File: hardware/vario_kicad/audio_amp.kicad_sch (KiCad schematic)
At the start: 16 parts

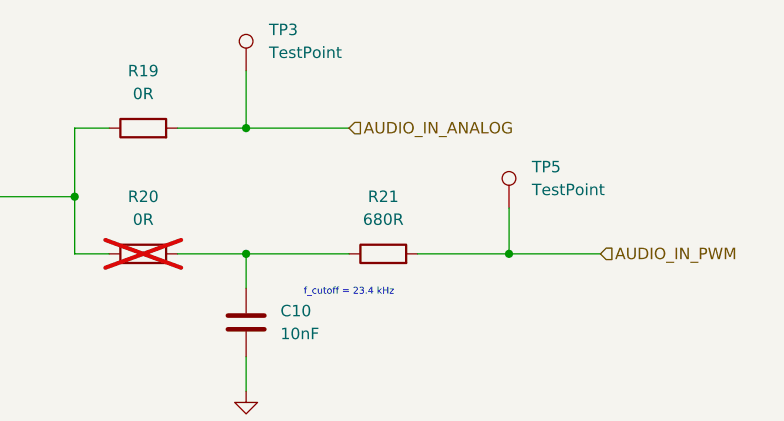
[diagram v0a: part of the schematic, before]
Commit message: remove more testpoints
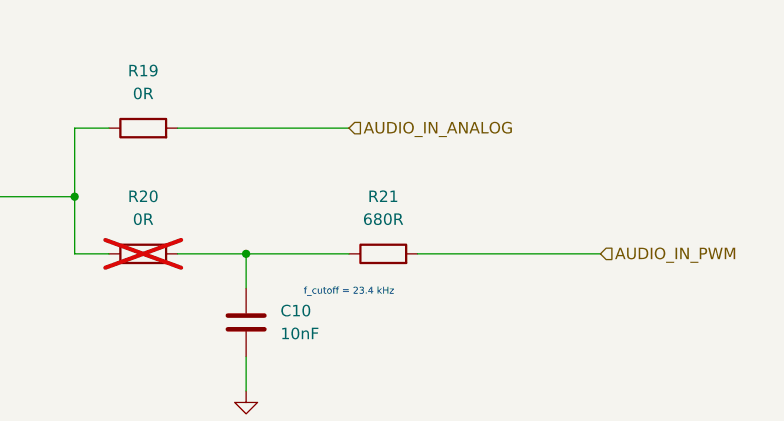
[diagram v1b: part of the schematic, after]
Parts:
- removed TP3, TP5: TestPoint, TestPoint:TestPoint_Pad_D1.0mm, symbol Connector:TestPoint
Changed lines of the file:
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@@
-	)
-	(junction
-		(at 226.06 97.79)
-		(diameter 0)
-		(color 0 0 0 0)
 	)
 	(junction
@@
 	)
 	(junction
-		(at 196.85 83.82)
-		(diameter 0)
-		(color 0 0 0 0)
-	)
-	(junction
 		(at 78.74 115.57)
 		(diameter 0)
@@
 	(wire
 		(pts
-			(xy 226.06 92.71) (xy 226.06 97.79)
-		)
-		(stroke
-			(width 0)
-			(type default)
-		)
-	)
-	(wire
-		(pts
 			(xy 68.58 100.33) (xy 60.96 100.33)
 		)
@@
 	(wire
 		(pts
-			(xy 226.06 97.79) (xy 236.22 97.79)
+			(xy 215.9 97.79) (xy 236.22 97.79)
 		)
 		(stroke
@@
 	(wire
 		(pts
-			(xy 196.85 83.82) (xy 208.28 83.82)
-		)
-		(stroke
-			(width 0)
-			(type default)
-		)
-	)
-	(wire
-		(pts
 			(xy 109.22 115.57) (xy 95.25 115.57)
 		)
@@
 	(wire
 		(pts
-			(xy 215.9 97.79) (xy 226.06 97.79)
-		)
-		(stroke
-			(width 0)
-			(type default)
-		)
-	)
-	(wire
-		(pts
 			(xy 95.25 114.3) (xy 95.25 115.57)
 		)
@@
 	(wire
 		(pts
-			(xy 196.85 77.47) (xy 196.85 83.82)
-		)
-		(stroke
-			(width 0)
-			(type default)
-		)
-	)
-	(wire
-		(pts
 			(xy 177.8 91.44) (xy 177.8 83.82)
 		)
@@
 	(wire
 		(pts
-			(xy 189.23 83.82) (xy 196.85 83.82)
+			(xy 189.23 83.82) (xy 208.28 83.82)
 		)
 		(stroke
@@
 	)
 	(symbol
-		(lib_id "Connector:TestPoint")
-		(at 226.06 92.71 0)
-		(unit 1)
-		(exclude_from_sim no)
-		(in_bom yes)
-		(on_board yes)
-		(dnp no)
-		(fields_autoplaced yes)
-		(property "Reference" "TP5"
-			(at 228.6 88.1379 0)
-			(effects
-				(font
-					(size 1.27 1.27)
-				)
-				(justify left)
-			)
-		)
-		(property "Value" "TestPoint"
-			(at 228.6 90.6779 0)
-			(effects
-				(font
-					(size 1.27 1.27)
-				)
-				(justify left)
-			)
-		)
-		(property "Footprint" "TestPoint:TestPoint_Pad_D1.0mm"
-			(at 231.14 92.71 0)
-			(effects
-				(font
-					(size 1.27 1.27)
-				)
-				(hide yes)
-			)
-		)
-		(property "Datasheet" "~"
-			(at 231.14 92.71 0)
-			(effects
-				(font
-					(size 1.27 1.27)
-				)
-				(hide yes)
-			)
-		)
-		(property "Description" "test point"
-			(at 226.06 92.71 0)
-			(effects
-				(font
-					(size 1.27 1.27)
-				)
-				(hide yes)
-			)
-		)
-		(pin "1"
-		)
-		(instances
-			(project ""
-				(path "/50389aff-b244-451e-8e3a-c5addd2215e1/c1ce8014-8ca1-4d8c-ab67-abb68a6156e7"
-					(reference "TP5")
-					(unit 1)
-				)
-			)
-		)
-	)
-	(symbol
 		(lib_id "New_Library:NS4150B")
 		(at 80.01 97.79 0)
@@
 					(unit 1)
 				)
-			)
-		)
-	)
-	(symbol
-		(lib_id "Connector:TestPoint")
-		(at 196.85 77.47 0)
-		(unit 1)
-		(exclude_from_sim no)
-		(in_bom yes)
-		(on_board yes)
-		(dnp no)
-		(fields_autoplaced yes)
-		(property "Reference" "TP3"
-			(at 199.39 72.8979 0)
-			(effects
-				(font
-					(size 1.27 1.27)
-				)
-				(justify left)
-			)
-		)
-		(property "Value" "TestPoint"
-			(at 199.39 75.4379 0)
-			(effects
-				(font
-					(size 1.27 1.27)
-				)
-				(justify left)
-			)
-		)
-		(property "Footprint" "TestPoint:TestPoint_Pad_D1.0mm"
-			(at 201.93 77.47 0)
-			(effects
-				(font
-					(size 1.27 1.27)
-				)
-				(hide yes)
-			)
-		)
-		(property "Datasheet" "~"
-			(at 201.93 77.47 0)
-			(effects
-				(font
-					(size 1.27 1.27)
-				)
-				(hide yes)
-			)
-		)
-		(property "Description" "test point"
-			(at 196.85 77.47 0)
-			(effects
-				(font
-					(size 1.27 1.27)
-				)
-				(hide yes)
-			)
-		)
-		(pin "1"
-		)
-		(instances
-			(project "vario_kicad"
-				(path "/50389aff-b244-451e-8e3a-c5addd2215e1/c1ce8014-8ca1-4d8c-ab67-abb68a6156e7"
-					(reference "TP3")
-					(unit 1)
-				)

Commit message: use 0402 instead of 0603 for almost all caps
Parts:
- C10, C5, C6, C7, C8, C9: footprint Capacitor_SMD:C_0603_1608Metric -> Capacitor_SMD:C_0402_1005Metric
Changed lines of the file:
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@@
 			)
 		)
-		(property "Footprint" "Capacitor_SMD:C_0603_1608Metric"
+		(property "Footprint" "Capacitor_SMD:C_0402_1005Metric"
 			(at 96.2152 114.3 0)
 			(effects
@@
 			)
 		)
-		(property "Footprint" "Capacitor_SMD:C_0603_1608Metric"
+		(property "Footprint" "Capacitor_SMD:C_0402_1005Metric"
 			(at 53.0352 88.9 0)
 			(effects
@@
 			)
 		)
-		(property "Footprint" "Capacitor_SMD:C_0603_1608Metric"
+		(property "Footprint" "Capacitor_SMD:C_0402_1005Metric"
 			(at 153.67 90.4748 0)
 			(effects
@@
 			)
 		)
-		(property "Footprint" "Capacitor_SMD:C_0603_1608Metric"
+		(property "Footprint" "Capacitor_SMD:C_0402_1005Metric"
 			(at 39.0652 88.9 0)
 			(effects
@@
 			)
 		)
-		(property "Footprint" "Capacitor_SMD:C_0603_1608Metric"
+		(property "Footprint" "Capacitor_SMD:C_0402_1005Metric"
 			(at 197.8152 109.22 0)
 			(effects
@@
 			)
 		)
-		(property "Footprint" "Capacitor_SMD:C_0603_1608Metric"
+		(property "Footprint" "Capacitor_SMD:C_0402_1005Metric"
 			(at 153.67 104.4448 0)
 			(effects
